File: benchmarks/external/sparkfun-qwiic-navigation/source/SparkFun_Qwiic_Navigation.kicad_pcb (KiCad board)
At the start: 2 copper layers, 25.4 x 25.4 mm, 68 parts, among them J1 Qwiic_RA, J2 Conn_01x04, J3 Qwiic_RA, J5 I2C, SW2 Nav Switch, U4 PCA9554PW

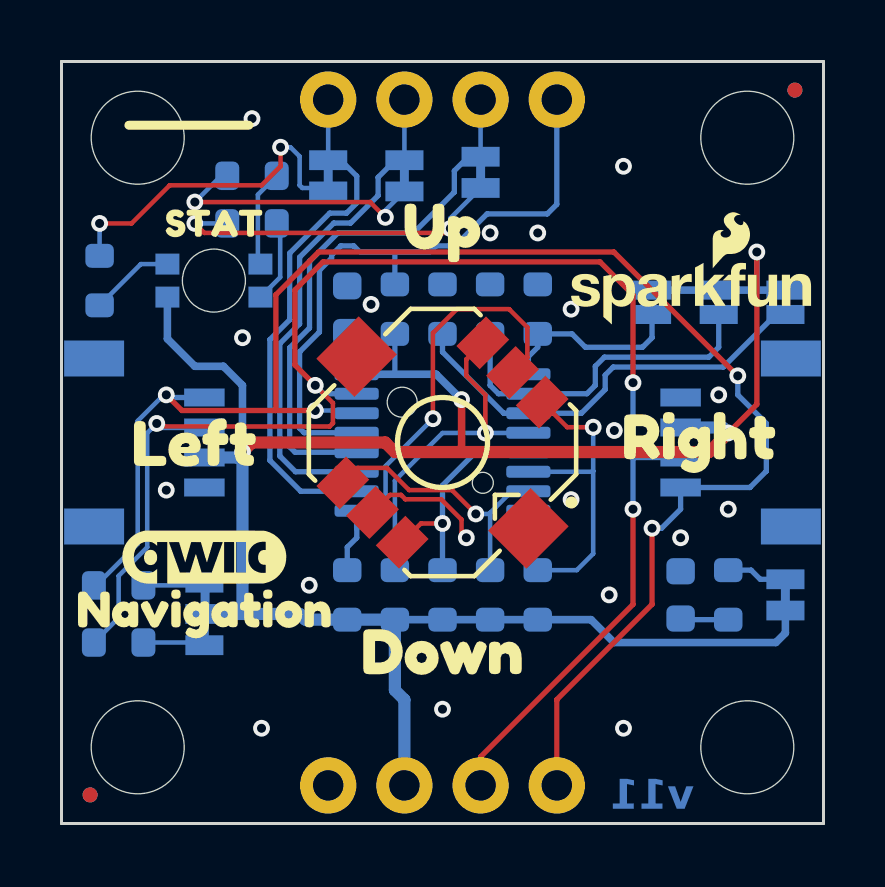
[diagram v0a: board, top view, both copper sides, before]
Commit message: test(fixtures): introduce controlled F.Cu short for KiCad source-marker acceptance
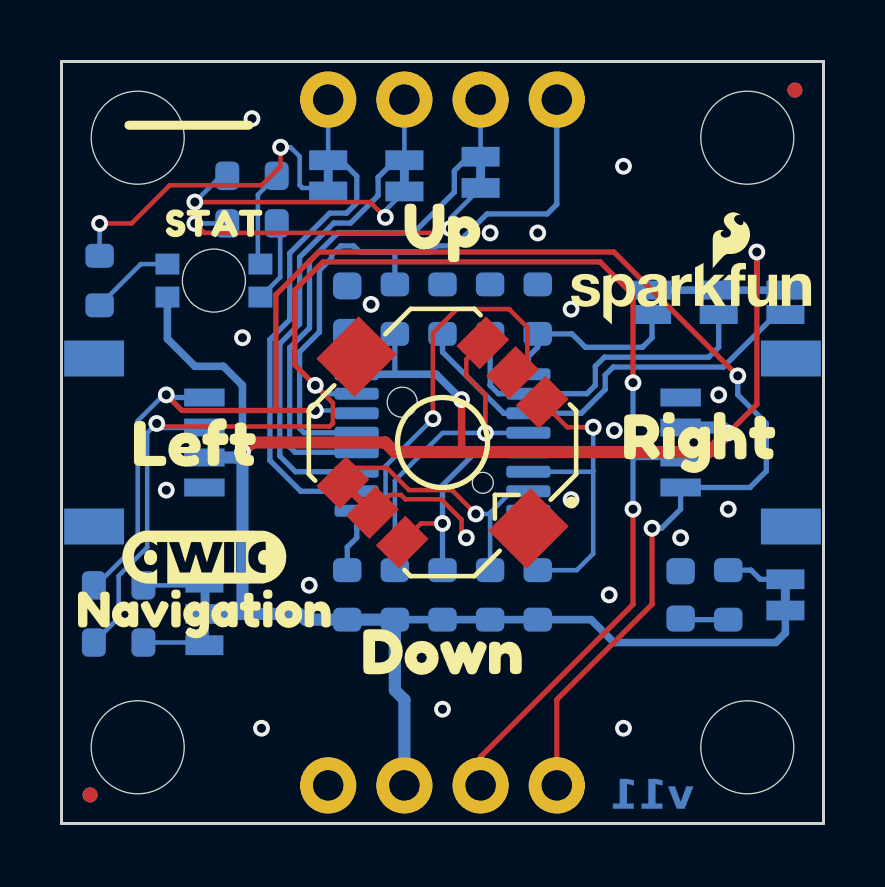
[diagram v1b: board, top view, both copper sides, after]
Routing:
- net SW_Left: track 9.25 -> 10.6 mm
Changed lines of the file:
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@@
 		(layer "F.SilkS")
 	)
+	(segment
+		(start 144.631598 106.118503)
+		(end 145.621548 107.108452)
+		(width 0.25)
+		(layer "F.Cu")
+		(net 18)
+	)
 )
